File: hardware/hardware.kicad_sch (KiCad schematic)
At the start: 32 parts, among them J1 120V, J2 USB_B, J3 temp0, J4 temp1, J5 heat0, J6 heat1, SW1 BOOT, SW2 RST, U1 AZ1117CR-3.3, U2 ESP32-C3-MINI-1U

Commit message: layout WIP
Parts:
- TP1, TP2: footprint TestPoint:TestPoint_Plated_Hole_D2.0mm -> TestPoint:TestPoint_THTPad_D1.0mm_Drill0.5mm
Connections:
- net 120V_HOT: now also J1.2 (Pin_2); no longer J1.3 (Pin_3)
- net 120V_NEUTRAL: now also J1.3 (Pin_3), J5.2 (Pin_2); no longer J1.2 (Pin_2), J5.1 (Pin_1)
- net CS1: now also U2.6 (GPIO3/ADC1_CH3); no longer U2.16 (GPIO10)
- net HEAT0: now also U2.21 (GPIO7); no longer U2.18 (GPIO4/ADC1_CH4)
- net HEAT1: now also U2.20 (GPIO6); no longer U2.19 (GPIO5/ADC2_CH0)
- net LED: now also U2.19 (GPIO5/ADC2_CH0); no longer U2.20 (GPIO6)
- net MISO: now also U2.12 (GPIO0/ADC1_CH0/XTAL_32K_P); no longer U2.6 (GPIO3/ADC1_CH3)
- net SCK: now also U2.16 (GPIO10); no longer U2.12 (GPIO0/ADC1_CH0/XTAL_32K_P)
- net USB_D+: now also D1.2 (I/O1); no longer D1.3 (I/O2)
- net USB_D-: now also D1.3 (I/O2); no longer D1.2 (I/O1)
- net ZCD: now also U2.18 (GPIO4/ADC1_CH4); no longer U2.21 (GPIO7)
- net heater0/T1: now also J5.1 (Pin_1); no longer J5.2 (Pin_2)
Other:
- note removed: "TODO move as needed"
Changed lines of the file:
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@@
 (kicad_sch (version 20211123) (generator eeschema)
   (paper "A4")
+  (junction (at 67.31 59.69) (diameter 0) (color 0 0 0 0)
+  )
+  (junction (at 41.91 57.15) (diameter 0) (color 0 0 0 0)
+  )
   (junction (at 120.65 26.67) (diameter 0) (color 0 0 0 0)
   )
@@
   (junction (at 73.66 33.02) (diameter 0) (color 0 0 0 0)
   )
-  (junction (at 41.91 59.69) (diameter 0) (color 0 0 0 0)
-  )
   (junction (at 181.61 121.92) (diameter 0) (color 0 0 0 0)
   )
   (junction (at 181.61 127) (diameter 0) (color 0 0 0 0)
   )
-  (junction (at 67.31 57.15) (diameter 0) (color 0 0 0 0)
-  )
   (junction (at 72.39 59.69) (diameter 0) (color 0 0 0 0)
   )
@@
     (stroke (width 0) (type default) (color 0 0 0 0))
   )
+  (wire (pts (xy 34.29 30.48) (xy 50.8 30.48))
+    (stroke (width 0) (type default) (color 0 0 0 0))
+  )
   (wire (pts (xy 35.56 114.3) (xy 36.83 114.3))
     (stroke (width 0) (type default) (color 0 0 0 0))
@@
     (stroke (width 0) (type default) (color 0 0 0 0))
   )
-  (wire (pts (xy 34.29 27.94) (xy 50.8 27.94))
-    (stroke (width 0) (type default) (color 0 0 0 0))
-  )
   (wire (pts (xy 87.63 27.94) (xy 87.63 25.4))
     (stroke (width 0) (type default) (color 0 0 0 0))
@@
     (stroke (width 0) (type default) (color 0 0 0 0))
   )
+  (wire (pts (xy 49.53 33.02) (xy 50.8 33.02))
+    (stroke (width 0) (type default) (color 0 0 0 0))
+  )
+  (wire (pts (xy 34.29 27.94) (xy 49.53 27.94))
+    (stroke (width 0) (type default) (color 0 0 0 0))
+  )
   (wire (pts (xy 35.56 33.02) (xy 35.56 34.29))
     (stroke (width 0) (type default) (color 0 0 0 0))
@@
     (stroke (width 0) (type default) (color 0 0 0 0))
   )
+  (wire (pts (xy 41.91 74.93) (xy 41.91 57.15))
+    (stroke (width 0) (type default) (color 0 0 0 0))
+  )
   (wire (pts (xy 85.09 114.3) (xy 85.09 113.03))
     (stroke (width 0) (type default) (color 0 0 0 0))
@@
     (stroke (width 0) (type default) (color 0 0 0 0))
   )
-  (wire (pts (xy 50.8 30.48) (xy 50.8 33.02))
-    (stroke (width 0) (type default) (color 0 0 0 0))
-  )
   (wire (pts (xy 31.75 67.31) (xy 33.02 67.31))
     (stroke (width 0) (type default) (color 0 0 0 0))
@@
     (stroke (width 0) (type default) (color 0 0 0 0))
   )
+  (wire (pts (xy 67.31 59.69) (xy 72.39 59.69))
+    (stroke (width 0) (type default) (color 0 0 0 0))
+  )
   (wire (pts (xy 54.61 106.68) (xy 54.61 107.95))
     (stroke (width 0) (type default) (color 0 0 0 0))
@@
     (stroke (width 0) (type default) (color 0 0 0 0))
   )
-  (wire (pts (xy 40.64 59.69) (xy 41.91 59.69))
+  (wire (pts (xy 40.64 59.69) (xy 67.31 59.69))
     (stroke (width 0) (type default) (color 0 0 0 0))
   )
@@
     (stroke (width 0) (type default) (color 0 0 0 0))
   )
-  (wire (pts (xy 41.91 59.69) (xy 72.39 59.69))
-    (stroke (width 0) (type default) (color 0 0 0 0))
-  )
   (wire (pts (xy 120.65 127) (xy 120.65 128.27))
     (stroke (width 0) (type default) (color 0 0 0 0))
@@
     (stroke (width 0) (type default) (color 0 0 0 0))
   )
-  (wire (pts (xy 40.64 57.15) (xy 67.31 57.15))
+  (wire (pts (xy 40.64 57.15) (xy 41.91 57.15))
     (stroke (width 0) (type default) (color 0 0 0 0))
   )
@@
     (stroke (width 0) (type default) (color 0 0 0 0))
   )
+  (wire (pts (xy 50.8 30.48) (xy 50.8 27.94))
+    (stroke (width 0) (type default) (color 0 0 0 0))
+  )
   (wire (pts (xy 133.35 38.1) (xy 133.35 39.37))
     (stroke (width 0) (type default) (color 0 0 0 0))
@@
     (stroke (width 0) (type default) (color 0 0 0 0))
   )
-  (wire (pts (xy 67.31 57.15) (xy 81.28 57.15))
+  (wire (pts (xy 49.53 27.94) (xy 49.53 33.02))
+    (stroke (width 0) (type default) (color 0 0 0 0))
+  )
+  (wire (pts (xy 41.91 57.15) (xy 81.28 57.15))
     (stroke (width 0) (type default) (color 0 0 0 0))
   )
@@
     (stroke (width 0) (type default) (color 0 0 0 0))
   )
-  (wire (pts (xy 41.91 59.69) (xy 41.91 74.93))
+  (wire (pts (xy 67.31 59.69) (xy 67.31 74.93))
     (stroke (width 0) (type default) (color 0 0 0 0))
   )
@@
     (stroke (width 0) (type default) (color 0 0 0 0))
   )
-  (wire (pts (xy 34.29 30.48) (xy 50.8 30.48))
-    (stroke (width 0) (type default) (color 0 0 0 0))
-  )
   (wire (pts (xy 100.33 25.4) (xy 100.33 26.67))
     (stroke (width 0) (type default) (color 0 0 0 0))
@@
     (stroke (width 0) (type default) (color 0 0 0 0))
   )
-  (wire (pts (xy 67.31 57.15) (xy 67.31 74.93))
-    (stroke (width 0) (type default) (color 0 0 0 0))
-  )
   (wire (pts (xy 81.28 57.15) (xy 87.63 57.15))
     (stroke (width 0) (type default) (color 0 0 0 0))
@@
   (wire (pts (xy 90.17 52.07) (xy 90.17 49.53))
     (stroke (width 0) (type default) (color 0 0 0 0))
-  )
-  (text "TODO move as needed" (at 95.25 95.25 0)
-    (effects (font (size 1.27 1.27)) (justify left bottom))
   )
   (label "120V_HOT" (at 217.17 87.63 180)
@@
     (effects (font (size 1.27 1.27)) (justify right bottom))
   )
-  (label "HEAT1" (at 125.73 99.06 180)
+  (label "HEAT1" (at 125.73 101.6 180)
     (effects (font (size 1.27 1.27)) (justify right bottom))
   )
@@
     (effects (font (size 1.27 1.27)) (justify left bottom))
   )
-  (label "MISO" (at 125.73 86.36 180)
+  (label "MISO" (at 125.73 88.9 180)
     (effects (font (size 1.27 1.27)) (justify right bottom))
   )
@@
     (effects (font (size 1.27 1.27)) (justify right bottom))
   )
-  (label "120V_NEUTRAL" (at 34.29 30.48 0)
+  (label "120V_NEUTRAL" (at 34.29 27.94 0)
     (effects (font (size 1.27 1.27)) (justify left bottom))
   )
@@
     (effects (font (size 1.27 1.27)) (justify right bottom))
   )
-  (label "HEAT0" (at 125.73 96.52 180)
-    (effects (font (size 1.27 1.27)) (justify right bottom))
-  )
-  (label "120V_HOT" (at 34.29 27.94 0)
+  (label "HEAT0" (at 125.73 104.14 180)
+    (effects (font (size 1.27 1.27)) (justify right bottom))
+  )
+  (label "120V_HOT" (at 34.29 30.48 0)
     (effects (font (size 1.27 1.27)) (justify left bottom))
   )
@@
     (effects (font (size 1.27 1.27)) (justify right bottom))
   )
-  (label "ZCD" (at 125.73 104.14 180)
-    (effects (font (size 1.27 1.27)) (justify right bottom))
-  )
-  (label "LED" (at 125.73 101.6 180)
+  (label "ZCD" (at 125.73 96.52 180)
+    (effects (font (size 1.27 1.27)) (justify right bottom))
+  )
+  (label "LED" (at 125.73 99.06 180)
     (effects (font (size 1.27 1.27)) (justify right bottom))
   )
@@
     (effects (font (size 1.27 1.27)) (justify left bottom))
   )
-  (label "CS1" (at 125.73 93.98 180)
+  (label "CS1" (at 125.73 86.36 180)
     (effects (font (size 1.27 1.27)) (justify right bottom))
   )
@@
     (effects (font (size 1.27 1.27)) (justify left bottom))
   )
-  (label "SCK" (at 125.73 88.9 180)
+  (label "SCK" (at 125.73 93.98 180)
     (effects (font (size 1.27 1.27)) (justify right bottom))
   )
@@
     (property "Reference" "TP1" (id 0) (at 119.38 118.11 90))
     (property "Value" "RX" (id 1) (at 124.46 118.11 90))
-    (property "Footprint" "TestPoint:TestPoint_Plated_Hole_D2.0mm" (id 2) (at 125.73 114.3 0)
+    (property "Footprint" "TestPoint:TestPoint_THTPad_D1.0mm_Drill0.5mm" (id 2) (at 125.73 114.3 0)
       (effects (font (size 1.27 1.27)) hide)
     )
@@
     (pin "2")
   )
-  (symbol (lib_id "Connector_Generic:Conn_01x02") (at 250.19 59.69 0) (mirror x) (unit 1)
-    (in_bom yes) (on_board yes) (fields_autoplaced)
-    (property "Reference" "J5" (id 0) (at 250.19 51.9135 0))
-    (property "Value" "heat0" (id 1) (at 250.19 54.6886 0))
-    (property "Footprint" "extraparts:Molex_MicroFit+_RH_1row_2pin" (id 2) (at 250.19 59.69 0)
-      (effects (font (size 1.27 1.27)) hide)
-    )
-    (property "Datasheet" "~" (id 3) (at 250.19 59.69 0)
+  (symbol (lib_id "Connector_Generic:Conn_01x02") (at 250.19 57.15 0) (unit 1)
+    (in_bom yes) (on_board yes)
+    (property "Reference" "J5" (id 0) (at 248.92 52.07 0)
+      (effects (font (size 1.27 1.27)) (justify left))
+    )
+    (property "Value" "heat0" (id 1) (at 247.65 54.61 0)
+      (effects (font (size 1.27 1.27)) (justify left))
+    )
+    (property "Footprint" "extraparts:Molex_MicroFit+_RH_1row_2pin" (id 2) (at 250.19 57.15 0)
+      (effects (font (size 1.27 1.27)) hide)
+    )
+    (property "Datasheet" "~" (id 3) (at 250.19 57.15 0)
       (effects (font (size 1.27 1.27)) hide)
     )
@@
     (property "Reference" "TP2" (id 0) (at 119.38 120.65 90))
     (property "Value" "TX" (id 1) (at 124.46 120.65 90))
-    (property "Footprint" "TestPoint:TestPoint_Plated_Hole_D2.0mm" (id 2) (at 125.73 116.84 0)
+    (property "Footprint" "TestPoint:TestPoint_THTPad_D1.0mm_Drill0.5mm" (id 2) (at 125.73 116.84 0)
       (effects (font (size 1.27 1.27)) hide)
     )
@@
     )
     (path "/174c1458-1006-404f-bb6a-5c79cd9829c4"
-      (reference "TP1") (unit 1) (value "RX") (footprint "TestPoint:TestPoint_Plated_Hole_D2.0mm")
+      (reference "TP1") (unit 1) (value "RX") (footprint "TestPoint:TestPoint_THTPad_D1.0mm_Drill0.5mm")
     )
     (path "/f3d8f89a-796a-468c-834f-cec0e76851e3"
-      (reference "TP2") (unit 1) (value "TX") (footprint "TestPoint:TestPoint_Plated_Hole_D2.0mm")
+      (reference "TP2") (unit 1) (value "TX") (footprint "TestPoint:TestPoint_THTPad_D1.0mm_Drill0.5mm")
     )
     (path "/c52db99c-b47a-411f-b853-c5e69444a7fd"

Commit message: finished layout
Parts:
- TP1, TP2: footprint TestPoint:TestPoint_THTPad_D1.0mm_Drill0.5mm -> TestPoint:TestPoint_Pad_D2.0mm
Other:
- sheet ZCD ports: added AC1, AC2; removed AC(L), AC(N)
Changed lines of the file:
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@@
     (stroke (width 0) (type default) (color 0 0 0 0))
   )
-  (label "120V_HOT" (at 217.17 87.63 180)
+  (label "120V_HOT" (at 217.17 90.17 180)
     (effects (font (size 1.27 1.27)) (justify right bottom))
   )
@@
     (effects (font (size 1.27 1.27)) (justify right bottom))
   )
-  (label "120V_NEUTRAL" (at 217.17 90.17 180)
+  (label "120V_NEUTRAL" (at 217.17 87.63 180)
     (effects (font (size 1.27 1.27)) (justify right bottom))
   )
@@
     (property "Reference" "TP1" (id 0) (at 119.38 118.11 90))
     (property "Value" "RX" (id 1) (at 124.46 118.11 90))
-    (property "Footprint" "TestPoint:TestPoint_THTPad_D1.0mm_Drill0.5mm" (id 2) (at 125.73 114.3 0)
+    (property "Footprint" "TestPoint:TestPoint_Pad_D2.0mm" (id 2) (at 125.73 114.3 0)
       (effects (font (size 1.27 1.27)) hide)
     )
@@
     (property "Reference" "TP2" (id 0) (at 119.38 120.65 90))
     (property "Value" "TX" (id 1) (at 124.46 120.65 90))
-    (property "Footprint" "TestPoint:TestPoint_THTPad_D1.0mm_Drill0.5mm" (id 2) (at 125.73 116.84 0)
+    (property "Footprint" "TestPoint:TestPoint_Pad_D2.0mm" (id 2) (at 125.73 116.84 0)
       (effects (font (size 1.27 1.27)) hide)
     )
@@
       (effects (font (size 1.27 1.27)) (justify right))
     )
-    (pin "AC(L)" input (at 217.17 87.63 180)
-      (effects (font (size 1.27 1.27)) (justify left))
-    )
-    (pin "AC(N)" input (at 217.17 90.17 180)
+    (pin "AC1" input (at 217.17 87.63 180)
+      (effects (font (size 1.27 1.27)) (justify left))
+    )
+    (pin "AC2" input (at 217.17 90.17 180)
       (effects (font (size 1.27 1.27)) (justify left))
     )
@@
     )
     (path "/174c1458-1006-404f-bb6a-5c79cd9829c4"
-      (reference "TP1") (unit 1) (value "RX") (footprint "TestPoint:TestPoint_THTPad_D1.0mm_Drill0.5mm")
+      (reference "TP1") (unit 1) (value "RX") (footprint "TestPoint:TestPoint_Pad_D2.0mm")
     )
     (path "/f3d8f89a-796a-468c-834f-cec0e76851e3"
-      (reference "TP2") (unit 1) (value "TX") (footprint "TestPoint:TestPoint_THTPad_D1.0mm_Drill0.5mm")
+      (reference "TP2") (unit 1) (value "TX") (footprint "TestPoint:TestPoint_Pad_D2.0mm")
     )
     (path "/c52db99c-b47a-411f-b853-c5e69444a7fd"

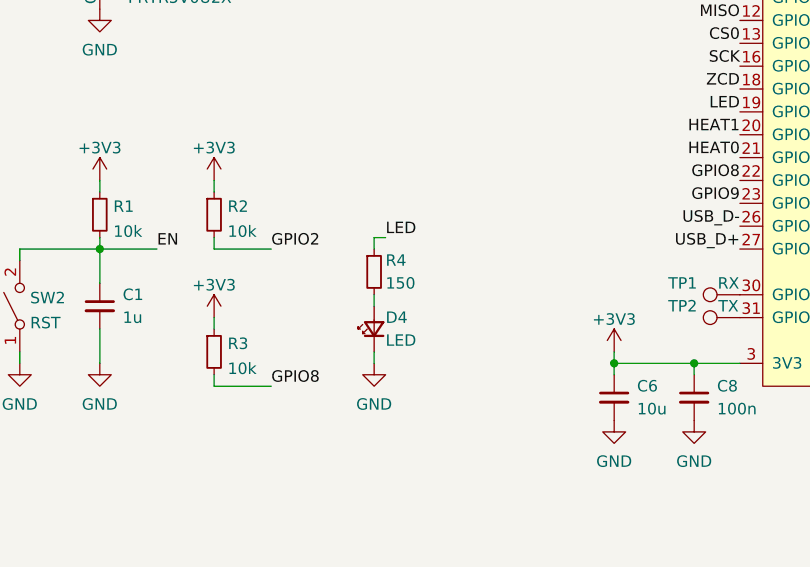
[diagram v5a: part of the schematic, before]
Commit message: basic testing except heater done
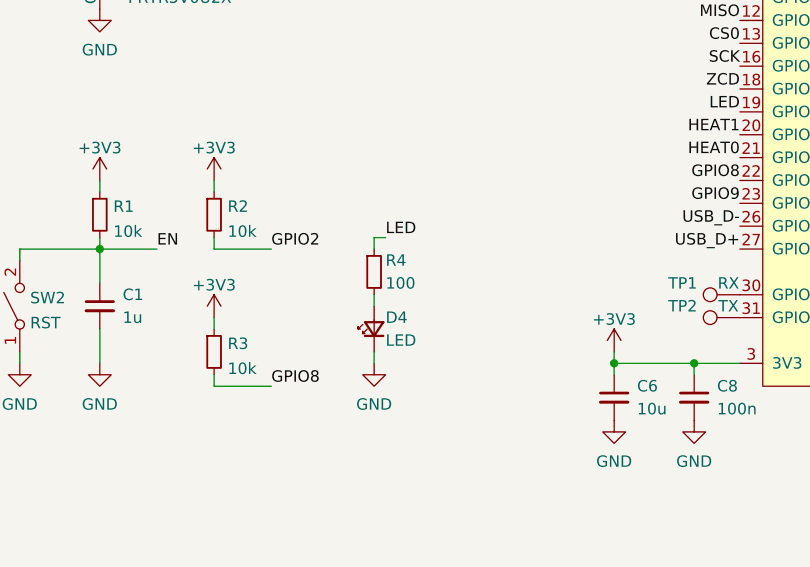
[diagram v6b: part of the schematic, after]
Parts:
- R4: value 150 -> 100
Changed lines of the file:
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@@
       (effects (font (size 1.27 1.27)) (justify left))
     )
-    (property "Value" "150" (id 1) (at 86.36 118.11 0)
+    (property "Value" "100" (id 1) (at 86.36 118.11 0)
       (effects (font (size 1.27 1.27)) (justify left))
     )
@@
     )
     (path "/903960c1-63c3-4ed1-ac6f-1d1a177eed00"
-      (reference "R4") (unit 1) (value "150") (footprint "Resistor_SMD:R_0603_1608Metric")
+      (reference "R4") (unit 1) (value "100") (footprint "Resistor_SMD:R_0603_1608Metric")
     )
     (path "/0165c157-e4a9-4485-9a52-09bc563c8c25"
@@
     )
     (path "/373f232b-89d5-460d-9d11-ed742c5707e1/947fc430-880a-43c2-bc6e-72029de3a25a"
-      (reference "R11") (unit 1) (value "150") (footprint "Resistor_SMD:R_0603_1608Metric")
+      (reference "R11") (unit 1) (value "100") (footprint "Resistor_SMD:R_0603_1608Metric")
     )
     (path "/373f232b-89d5-460d-9d11-ed742c5707e1/0c6987bd-0446-4772-a1bf-21a6fa732e72"
-      (reference "R12") (unit 1) (value "150") (footprint "Resistor_SMD:R_0603_1608Metric")
+      (reference "R12") (unit 1) (value "22") (footprint "Resistor_SMD:R_0603_1608Metric")
     )
     (path "/373f232b-89d5-460d-9d11-ed742c5707e1/91a6582d-c885-450f-87a6-af7126326a3e"
-      (reference "R13") (unit 1) (value "150") (footprint "Resistor_SMD:R_0603_1608Metric")
+      (reference "R13") (unit 1) (value "10k") (footprint "Resistor_SMD:R_0603_1608Metric")
     )
     (path "/bc5cc19f-b131-400c-ac42-ddb1ea322123/947fc430-880a-43c2-bc6e-72029de3a25a"
-      (reference "R14") (unit 1) (value "150") (footprint "Resistor_SMD:R_0603_1608Metric")
+      (reference "R14") (unit 1) (value "100") (footprint "Resistor_SMD:R_0603_1608Metric")
     )
     (path "/bc5cc19f-b131-400c-ac42-ddb1ea322123/0c6987bd-0446-4772-a1bf-21a6fa732e72"
-      (reference "R15") (unit 1) (value "150") (footprint "Resistor_SMD:R_0603_1608Metric")
+      (reference "R15") (unit 1) (value "22") (footprint "Resistor_SMD:R_0603_1608Metric")
     )
     (path "/bc5cc19f-b131-400c-ac42-ddb1ea322123/91a6582d-c885-450f-87a6-af7126326a3e"
-      (reference "R16") (unit 1) (value "150") (footprint "Resistor_SMD:R_0603_1608Metric")
+      (reference "R16") (unit 1) (value "10k") (footprint "Resistor_SMD:R_0603_1608Metric")
     )
     (path "/b49ac06c-52cb-4f6c-9d8c-7754c94a9167"
